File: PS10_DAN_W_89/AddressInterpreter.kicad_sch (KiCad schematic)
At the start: 4 parts, among them SW2 SW_DIP_x08, U19 MC14585, U20 MC14585

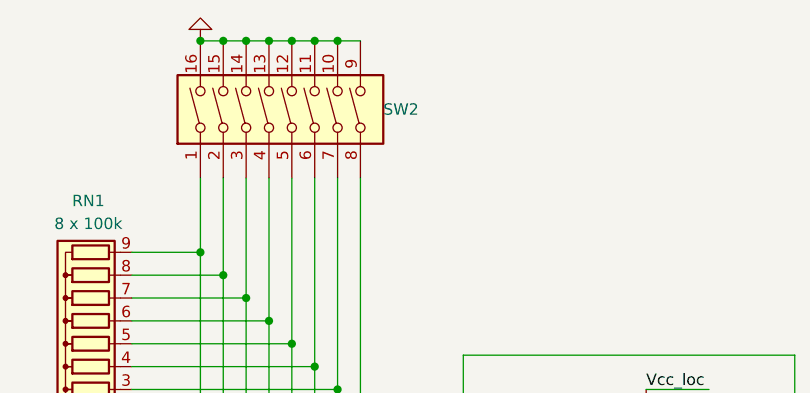
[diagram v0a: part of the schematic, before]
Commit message: Corrections in schematics made;
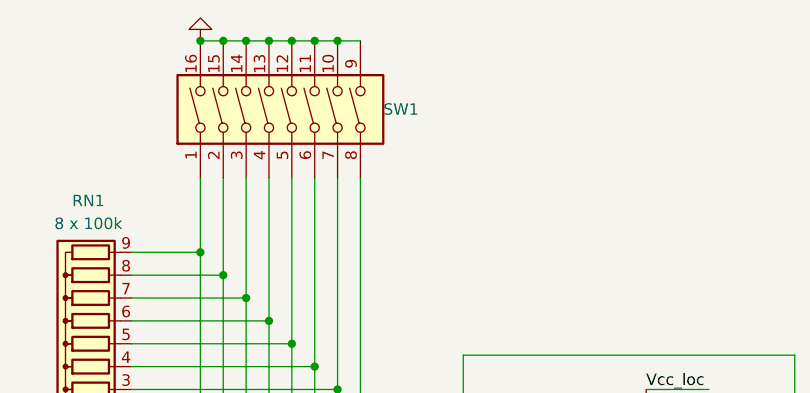
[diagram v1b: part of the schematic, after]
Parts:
- renumbered SW2 to SW1
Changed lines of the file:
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@@
   (symbol (lib_id "Switch:SW_DIP_x08") (at 134.62 33.02 90) (unit 1)
     (in_bom yes) (on_board yes) (dnp no)
-    (property "Reference" "SW2" (at 144.78 33.02 90)
+    (property "Reference" "SW1" (at 144.78 33.02 90)
       (effects (font (size 1.27 1.27)) (justify right))
     )
@@
       (project "PS10_DAN_W_89"
         (path "/e91a2aa5-4be5-4ade-bc4c-021deb2b0b30/ef79645b-0335-489a-98a9-236189d559b6"
-          (reference "SW2") (unit 1)
+          (reference "SW1") (unit 1)
         )
       )
